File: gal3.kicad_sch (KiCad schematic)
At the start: 8 parts, among them IC13 SN74ALS374N, IC8 SN74ALS374N, IC9 D65200GD076

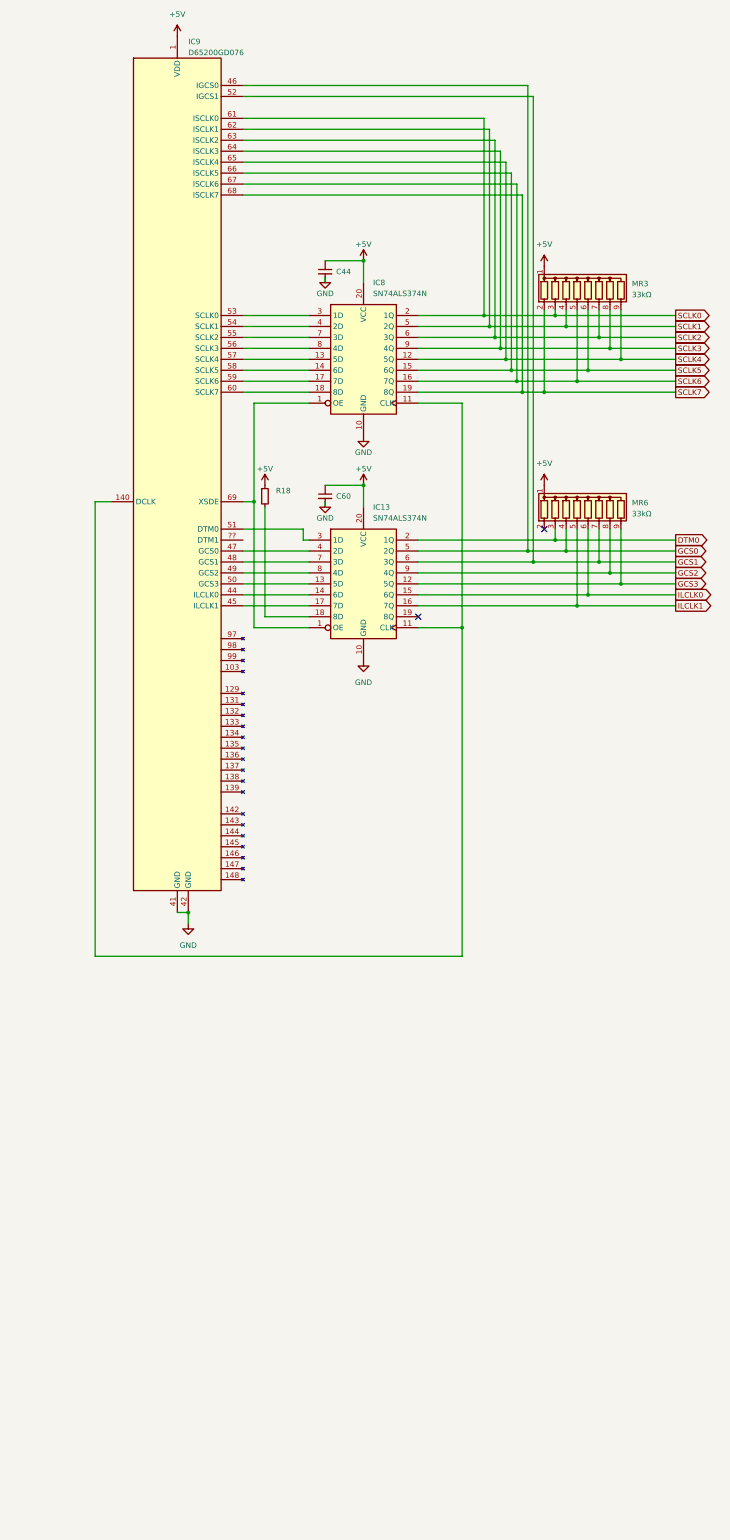
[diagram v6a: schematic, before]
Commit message: schematic: add lines between IC9 and GVRAM
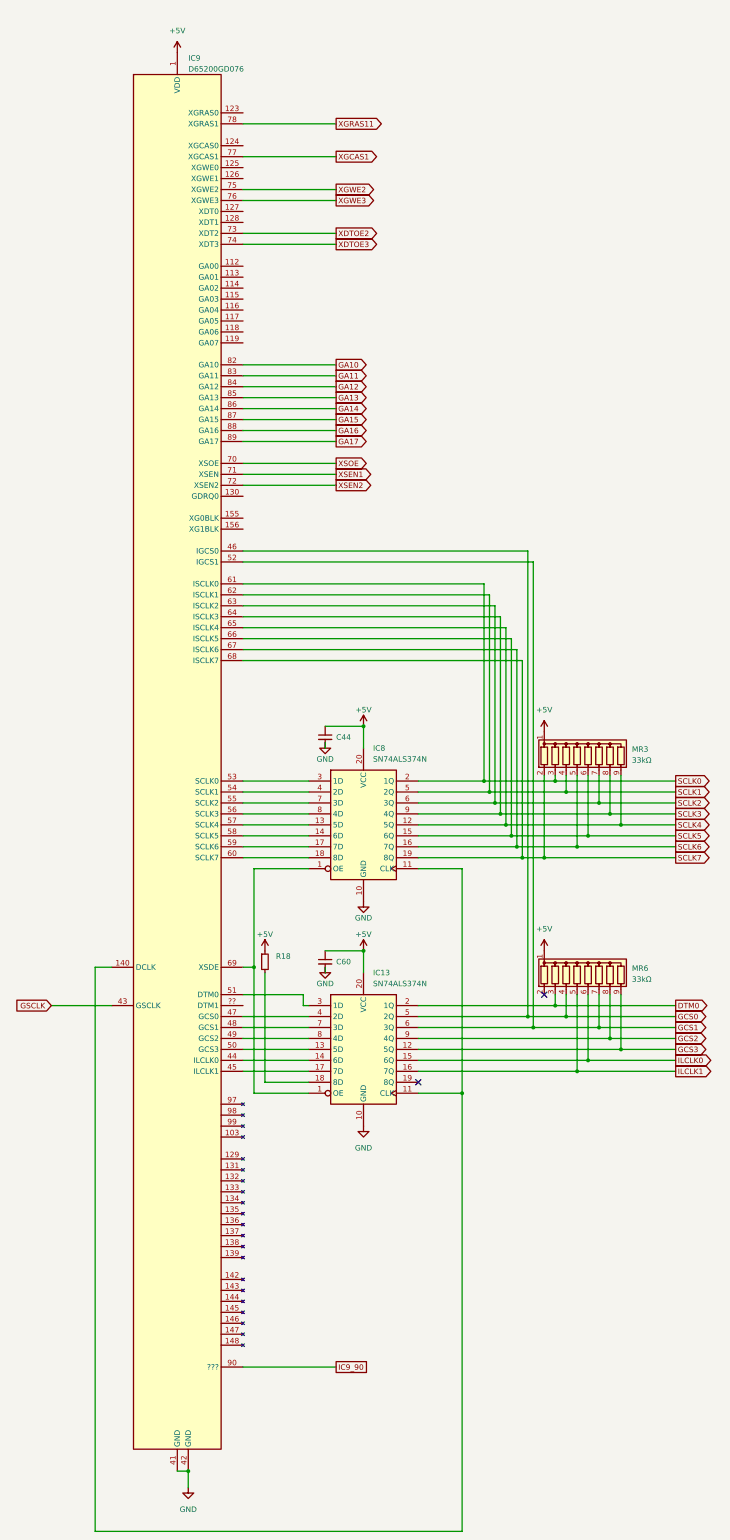
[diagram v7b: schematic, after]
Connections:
- new net GA10: IC9.82 (GA10)
- new net GA11: IC9.83 (GA11)
- new net GA12: IC9.84 (GA12)
- new net GA13: IC9.85 (GA13)
- new net GA14: IC9.86 (GA14)
- new net GA15: IC9.87 (GA15)
- new net GA16: IC9.88 (GA16)
- new net GA17: IC9.89 (GA17)
- new net GSCLK: IC9.43 (GSCLK)
- new net IC9_90: IC9.90 (???)
- new net XDTOE2: IC9.73 (XDT2)
- new net XDTOE3: IC9.74 (XDT3)
- new net XGCAS1: IC9.77 (XGCAS1)
- new net XGRAS11: IC9.78 (XGRAS1)
- new net XGWE2: IC9.75 (XGWE2)
- new net XGWE3: IC9.76 (XGWE3)
- new net XSEN1: IC9.71 (XSEN)
- new net XSEN2: IC9.72 (XSEN2)
- new net XSOE: IC9.70 (XSOE)
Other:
- moved on the sheet: C44, C60, IC13, IC8, MR3, MR6, R18

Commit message: schematic: add IC22, IC6
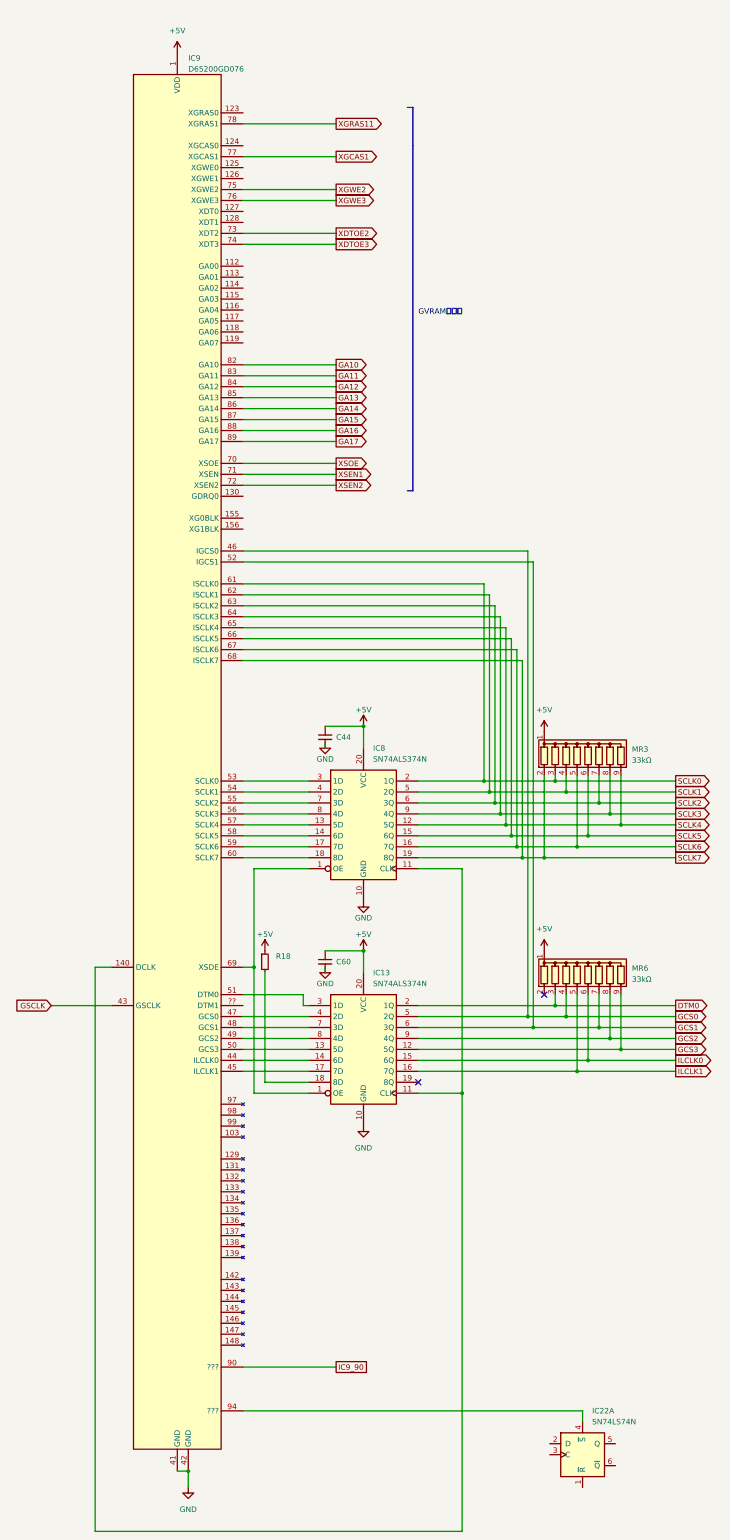
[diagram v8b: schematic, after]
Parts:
- added IC22: SN74LS74N, Package_DIP:DIP-14_W7.62mm, symbol 74xx:74LS74
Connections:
- new net: IC22.4 (~{S}), IC9.94 (???)
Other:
- note added: "GVRAMへ接続"
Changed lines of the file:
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@@
+    (stroke (width 0) (type default))
+  )
+  (polyline (pts (xy 106.68 139.7) (xy 106.68 59.69))
     (stroke (width 0) (type default))
   )
@@
     (stroke (width 0) (type default))
   )
+  (polyline (pts (xy 106.68 59.69) (xy 106.68 50.8))
+    (stroke (width 0) (type default))
+  )
   (wire (pts (xy 118.11 381) (xy 33.02 381))
     (stroke (width 0) (type default))
@@
     (stroke (width 0) (type default))
   )
+  (wire (pts (xy 67.31 353.06) (xy 146.05 353.06))
+    (stroke (width 0) (type default))
+  )
   (wire (pts (xy 125.73 212.09) (xy 149.86 212.09))
     (stroke (width 0) (type default))
@@
     (stroke (width 0) (type default))
   )
+  (polyline (pts (xy 105.41 139.7) (xy 106.68 139.7))
+    (stroke (width 0) (type default))
+  )
   (wire (pts (xy 67.31 123.19) (xy 88.9 123.19))
     (stroke (width 0) (type default))
@@
     (stroke (width 0) (type default))
   )
+  (polyline (pts (xy 105.41 50.8) (xy 106.68 50.8))
+    (stroke (width 0) (type default))
+  )
   (wire (pts (xy 81.28 259.08) (xy 81.28 256.54))
     (stroke (width 0) (type default))
@@
     (stroke (width 0) (type default))
   )
+  (wire (pts (xy 146.05 353.06) (xy 146.05 355.6))
+    (stroke (width 0) (type default))
+  )
   (wire (pts (xy 67.31 224.79) (xy 82.55 224.79))
     (stroke (width 0) (type default))
@@
   (wire (pts (xy 124.46 163.83) (xy 124.46 209.55))
     (stroke (width 0) (type default))
+  )
+  (text "GVRAMへ接続" (at 107.95 99.06 0)
+    (effects (font (size 1.27 1.27)) (justify left bottom))
   )
   (global_label "GA17" (shape output) (at 88.9 128.27 0) (fields_autoplaced)
@@
     (pin "123")
     (pin "90")
+    (pin "94")
     (instances
       (project "88va2-circuit"
@@
         )
       )
+    )
+  )
+  (symbol (lib_id "74xx:74LS74") (at 146.05 363.22 0) (unit 1)
+    (in_bom yes) (on_board yes) (dnp no) (fields_autoplaced)
+    (property "Reference" "IC22" (at 148.2441 353.06 0)
+      (effects (font (size 1.27 1.27)) (justify left))
+    )
+    (property "Value" "SN74LS74N" (at 148.2441 355.6 0)
+      (effects (font (size 1.27 1.27)) (justify left))
+    )
+    (property "Footprint" "Package_DIP:DIP-14_W7.62mm" (at 146.05 363.22 0)
+      (effects (font (size 1.27 1.27)) hide)
+    )
+    (property "Datasheet" "74xx/74hc_hct74.pdf" (at 146.05 363.22 0)
+      (effects (font (size 1.27 1.27)) hide)
+    )
+    (pin "3")
+    (pin "10")
+    (pin "4")
+    (pin "1")
+    (pin "11")
+    (pin "13")
+    (pin "14")
+    (pin "6")
+    (pin "12")
+    (pin "8")
+    (pin "9")
+    (pin "7")
+    (pin "5")
+    (pin "2")
+    (instances
+      (project "88va2-circuit"
+        (path "/8cd193ae-a369-4130-9ba4-f2075fa60e2b/69b5e096-b79d-4084-a9d7-aa17e9aa2515"
+          (reference "IC22") (unit 1)
+        )
+      )
